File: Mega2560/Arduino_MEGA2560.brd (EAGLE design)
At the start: 81.5 x 53.3 mm, 8 parts

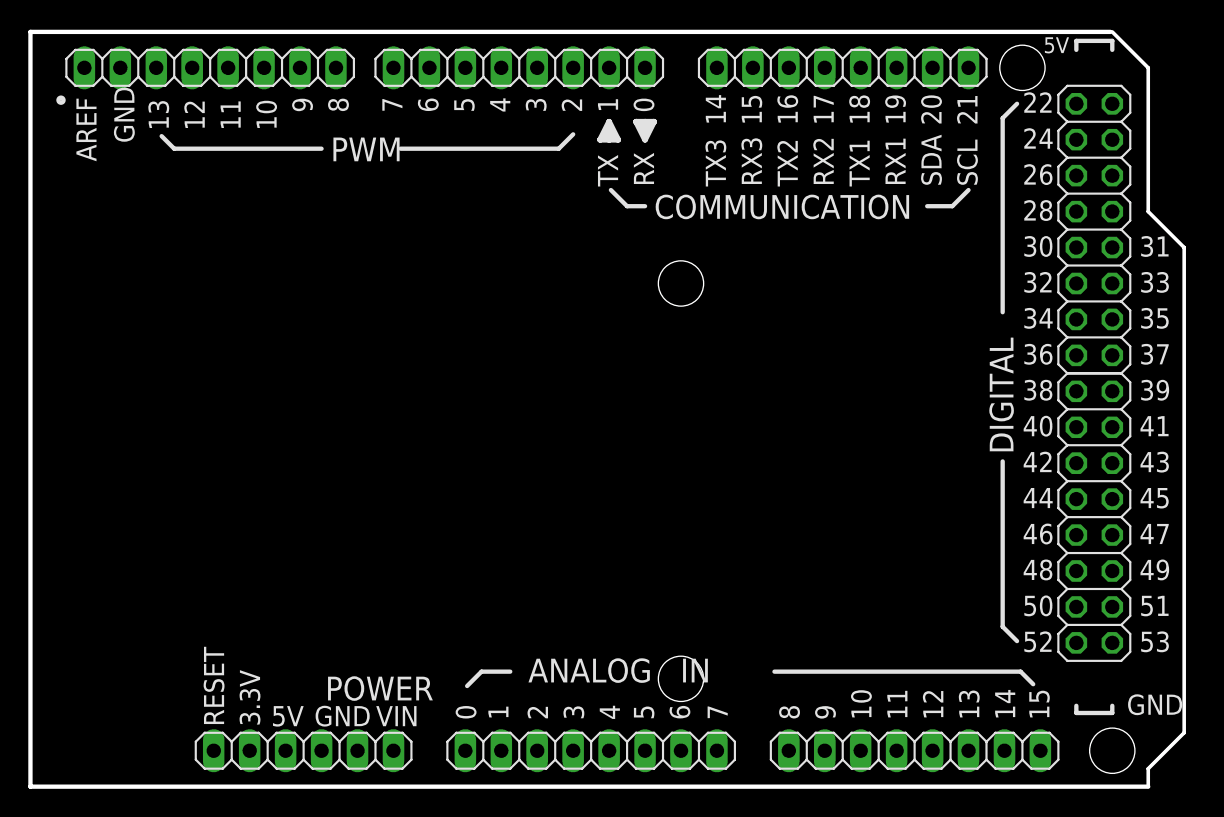
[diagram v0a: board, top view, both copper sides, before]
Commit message: Arduino added ground pours
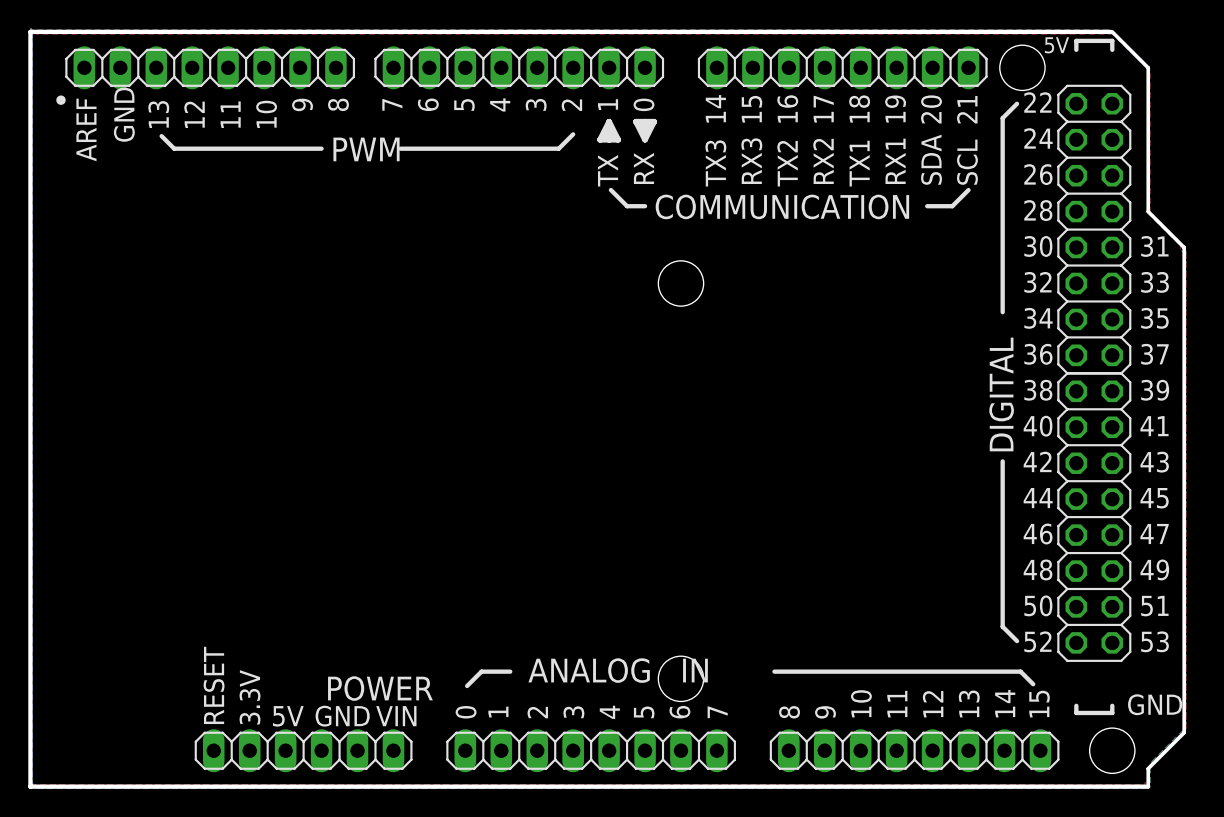
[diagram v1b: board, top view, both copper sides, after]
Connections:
- new net GND: POWER.4, POWER.5, PWMH.7
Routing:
- added copper zone on layer 1, net GND
- added copper zone on layer 16, net GND
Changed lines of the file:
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@@
 </elements>
 <signals>
+<signal name="GND">
+<contactref element="POWER" pad="4"/>
+<contactref element="POWER" pad="5"/>
+<polygon width="0.4064" layer="16">
+<vertex x="20.193" y="53.34"/>
+<vertex x="20.193" y="0.254"/>
+<vertex x="20.574" y="-0.127"/>
+<vertex x="98.806" y="-0.127"/>
+<vertex x="99.187" y="0.254"/>
+<vertex x="99.187" y="1.397"/>
+<vertex x="99.314" y="1.524"/>
+<vertex x="99.314" y="1.778"/>
+<vertex x="101.727" y="4.191"/>
+<vertex x="101.727" y="37.846"/>
+<vertex x="99.06" y="40.513"/>
+<vertex x="99.06" y="50.673"/>
+<vertex x="96.266" y="53.467"/>
+<vertex x="20.193" y="53.467"/>
+<vertex x="20.066" y="53.594"/>
+</polygon>
+<polygon width="0.4064" layer="1">
+<vertex x="20.066" y="53.34"/>
+<vertex x="20.066" y="0.127"/>
+<vertex x="98.806" y="0.127"/>
+<vertex x="98.806" y="0.254"/>
+<vertex x="99.06" y="0.254"/>
+<vertex x="99.06" y="1.143"/>
+<vertex x="99.06" y="1.397"/>
+<vertex x="101.727" y="4.064"/>
+<vertex x="101.727" y="37.592"/>
+<vertex x="101.346" y="37.973"/>
+<vertex x="101.346" y="38.354"/>
+<vertex x="99.187" y="40.513"/>
+<vertex x="99.187" y="50.673"/>
+<vertex x="98.806" y="51.054"/>
+<vertex x="96.647" y="53.213"/>
+<vertex x="20.447" y="53.213"/>
+<vertex x="20.32" y="53.34"/>
+<vertex x="20.193" y="53.34"/>
+<vertex x="20.066" y="53.467"/>
+</polygon>
+<contactref element="PWMH" pad="7"/>
+</signal>
 </signals>
 <errors>
